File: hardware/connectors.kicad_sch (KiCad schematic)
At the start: 22 parts, among them IC1 API7721FSB-13, J1 FTSH-107-01-L-D-K, J2 USB_C_Receptacle_USB2.0_14P, J25 Conn_01x02, J26 Conn_01x02, J3 SMA, J4 SMA, J5 uFL, J6 uFL, J7 XIAO ESP32S3 Sense, U2 CP2102C-A01-GQFN24R

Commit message: Fixes after review
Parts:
- added C15: 100n, symbol Device:C_Small
- added C16: C_Small, symbol Device:C_Small
- added C17, C26, C27: 10n, symbol Device:C_Small
- added C18, C19: 47p, symbol Device:C_Small
- added D6, D7: LED, symbol Device:LED
- added IC2: FT231XS-U, Package_SO:SSOP-20_3.9x8.7mm_P0.635mm, symbol FT231XS-U:FT231XS-U
- added R13, R14: 220R, symbol Device:R
- R2, R6: value 1k -> 27R
- R3, R4, R5, U2: now not fitted; now left out of the parts list
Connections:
- net +3.3V: now also C27.1
- net 3V3_USB: now also C15.1, C26.1, IC2.13 (3V3OUT), IC2.3 (VCCIO)
- net D+: now also C19.1, IC2.11 (USBDP)
- net D-: now also C18.1, IC2.12 (USBDM)
- net GND: now also C27.2, D6.1 (K), D7.1 (K); no longer J3.2 (Ext), J3.3 (Ext), J3.4 (Ext), J3.5 (Ext), J4.2 (Ext), J4.3 (Ext), J4.4 (Ext), J4.5 (Ext), J5.2 (Ext), J5.3 (Ext), J5.4 (Ext), J5.5 (Ext), J6.2 (Ext), J6.3 (Ext), J6.4 (Ext), J6.5 (Ext)
- net GND_USB: now also C15.2, C16.1, C17.2, C18.2, C19.2, C26.2, IC2.16 (GND_2), IC2.6 (GND_1)
- net ISO_RX: now also IC2.4 (RXD)
- net ISO_TX: now also IC2.20 (TXD)
- net VBUS: now also C17.1, IC2.15 (VCC)
- new net: D7.2 (A), R14.1
- new net: J6.2 (Ext), J6.3 (Ext), J6.4 (Ext), J6.5 (Ext)
- new net: D6.2 (A), R13.1
- new net: J5.2 (Ext), J5.3 (Ext), J5.4 (Ext), J5.5 (Ext)
- new net: J3.2 (Ext), J3.3 (Ext), J3.4 (Ext), J3.5 (Ext)
- new net: J4.2 (Ext), J4.3 (Ext), J4.4 (Ext), J4.5 (Ext)
- new net RXLED: IC2.10 (CBUS2), R13.2
- new net TXLED: IC2.17 (CBUS1), R14.2
- new net USB_RST: IC2.14 (RESET#)
- no-connect marks 27 -> 39
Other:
- note added: "backup if FT231XS will be out of stock"
- note removed: "Question 1 -------> If not these connectors below but Harwin, should I throw away all of these and copy Harwin from ams master? I am unsure about pins assignment, because frontbox has it completely different than ams master."
- moved on the sheet: D13, D14, D15, D2, D3, D4, IC1, J1, J25, J26, J3, J4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

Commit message: Added pi-filter to VANT and added socket for battery
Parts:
- D2: value ~ -> (none)

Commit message: Fixes after review and mouser links for most components added
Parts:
- removed C15: 100n, symbol Device:C_Small
- removed C16: C_Small, symbol Device:C_Small
- removed J2: USB_C_Receptacle_USB2.0_14P, symbol Connector:USB_C_Receptacle_USB2.0_14P
- removed R2, R6: 27R, symbol Device:R
- removed R3: 22.1k, symbol Device:R
- removed R4: 47.5k, symbol Device:R
- removed R5: 1k, symbol Device:R
- removed U2: CP2102C-A01-GQFN24R, QFN50P400X400X80-25N-D, symbol CP2102C-A01-GQFN24R:CP2102C-A01-GQFN24R
- added C13: 100nF, Capacitor_SMD:C_0603_1608Metric_Pad1.08x0.95mm_HandSolder, symbol Device:C_Small
- added D2, D8: SMF5.0A, 5Vtvs:SODFL3618X110N, symbol Diode:SMF5V0A
- added FB1: 40R@100MHz, FerriteUSB:BEADC2012X110N, symbol Device:FerriteBead_Small
- added J7: USB_A, USBAconnector:UE27AC5410H, symbol Connector:USB_A
- added R10, R11: 27R, Resistor_SMD:R_0603_1608Metric_Pad0.98x0.95mm_HandSolder, symbol Device:R
- added R12: 10k, Resistor_SMD:R_0603_1608Metric_Pad0.98x0.95mm_HandSolder, symbol Device:R
- C12: renamed from C17; value 10n -> 10nF; footprint (none) -> Capacitor_SMD:C_0603_1608Metric_Pad1.08x0.95mm_HandSolder; Mouser (none) -> https://www.mouser.pl/ProductDetail/Murata-Electronics/GCM1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
- C14: renamed from C26; value 10n -> 10nF; footprint (none) -> Capacitor_SMD:C_0603_1608Metric_Pad1.08x0.95mm_HandSolder; Mouser (none) -> https://www.mouser.pl/ProductDetail/Murata-Electronics/GCM1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
- C16: renamed from C27; value 10n -> 10nF; footprint (none) -> Capacitor_SMD:C_0603_1608Metric_Pad1.08x0.95mm_HandSolder; Mouser (none) -> https://www.mouser.pl/ProductDetail/Murata-Electronics/GCM1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
- C24: renamed from C18; value 47p -> 47pF; now not fitted
- C25: renamed from C19; value 47p -> 47pF; now not fitted
- D10: renamed from D14; value STS232050B751 -> 5V/360W
- D11: renamed from D15; value 3.6V/400W -> 3.6V/85W
- D6: renamed from D13; value STS232050B751 -> (none); footprint Package_TO_SOT_SMD:SOT-23_Handsoldering -> (none); Manufacturer_Part_Number STS232050B751 -> (none); Mouser https://www.mouser.pl/ProductDetail/Eaton-Electronics/STS23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 -> (none); Mouser No 504-STS232050B751 -> (none)
- D9: renamed from D4; value STS232050B751 -> 5V/360W
- J2: renamed from J5; value uFL -> uFL ant
- J3: value SMA -> SMA ant
- J4: renamed from J6; value uFL -> uFL ant
- J5: renamed from J4; value SMA -> SMA ant
- J9: renamed from J7; Mouser (none) -> ---
- R13, R14: value 220R -> 330R; footprint (none) -> Resistor_SMD:R_0603_1608Metric_Pad0.98x0.95mm_HandSolder; Mouser (none) -> https://www.mouser.pl/ProductDetail/Vishay-Draloric/RCS0603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
- U4: renamed from IC2; Mouser (none) -> https://www.mouser.pl/ProductDetail/FTDI/FT231XS-R?qs=Gp1Yz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
- U5: renamed from IC1; Mouser (none) -> https://www.mouser.pl/ProductDetail/Diodes-Incorporated/API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
- renumbered D2 to D3, D6 to D4, D7 to D5, D3 to D7, J25 to J1, J26 to J6, J1 to J8
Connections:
- net +5V: now also D8.1 (A1)
- net 3V3_USB: now also R13.2, R14.2, C13.1, R12.1
- net D+: now also J7.3 (D+), R11.2; no longer U4.11 (USBDP)
- net D-: now also J7.2 (D-), R10.2; no longer U4.12 (USBDM)
- net GND: now also D8.2 (A2); no longer D4.1 (K), D5.1 (K)
- net GND_USB: now also C13.2, D2.2 (A2), J7.4 (GND), J7.SH (Shield)
- net RXLED: now also D4.1 (K); no longer R13.2
- net TXLED: now also D5.1 (K); no longer R14.2
- net USB_RST: now also R12.2
- net VBUS: now also FB1.2; no longer C12.1
- net at J4.2 (Ext), J4.3 (Ext), J4.4 (Ext)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: now also J5.2 (Ext), J5.3 (Ext), J5.4 (Ext), J5.5 (Ext)
- net at J2.2 (Ext), J2.3 (Ext), J2.4 (Ext)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: now also J3.2 (Ext), J3.3 (Ext), J3.4 (Ext), J3.5 (Ext)
- new net: R10.1, U4.12 (USBDM)
- new net: C12.1, D2.1 (A1), FB1.1, J7.1 (VBUS)
- new net: R11.1, U4.11 (USBDP)
- no-connect marks 39 -> 21
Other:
- moved on the sheet: C12, D3, D4, D5, D7, J2, J3, J5, J9, R13, U4

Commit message: changed some elements on shematic
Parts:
- added D15, D16: SMF5.0A, 5Vtvs:SODFL3618X110N, symbol Diode:SMF5V0A
- C24, C25: footprint (none) -> DoNotPopulate; Mouser (none) -> --
- D3: value (none) -> 5V/140W; footprint (none) -> Package_TO_SOT_SMD:SOT-23-3; Mouser (none) -> https://www.mouser.pl/ProductDetail/STMicroelectronics/ESDA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
- D4, D5: footprint (none) -> Diode_SMD:D_0603_1608Metric_Pad1.05x0.95mm_HandSolder; Mouser (none) -> https://www.mouser.pl/ProductDetail/Wurth-Elektronik/150060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
- D6: value (none) -> 27V/420W; footprint (none) -> Package_TO_SOT_SMD:SOT-23-3; Mouser (none) -> https://www.mouser.pl/ProductDetail/Micro-Commercial-Compon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
- D7: Mouser (none) -> https://www.mouser.pl/ProductDetail/onsemi/NSVRB751V40T1G?q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; Mouser Part Number 863-NSVRB751V40T1G -> (none); Mouser Price/Stock https://www.mouser.pl/ProductDetail/onsemi/NSVRB751V40T1G?q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 -> (none)
- D8: value SMF5.0A -> 5V/200W
- J7: footprint USBAconnector:UE27AC5410H -> USBAconnector:UJ2AV4TH; Mouser https://www.mouser.pl/ProductDetail/Amphenol-Commercial-Pro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 -> https://www.mouser.pl/ProductDetail/Same-Sky/UJ2-AV-4-TH?qs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
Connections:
- net D+: no longer D3.2 (A2)
- net D-: no longer D3.1 (A1)
- net d-: now reaches R10.1, U4.12 (USBDM)
- net d-: now also D3.1 (A1)
- net d+: now reaches R11.1, U4.11 (USBDP)
- net d+: now also D3.2 (A2)
- net at J4.1 (In), J5.1 (In): now also D15.1 (A1)
- net at J4.2 (Ext), J4.3 (Ext), J4.4 (Ext)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: now also D15.2 (A2)
- net at J2.1 (In), J3.1 (In): now also D16.1 (A1)
- net at J2.2 (Ext), J2.3 (Ext), J2.4 (Ext)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: now also D16.2 (A2)
- net +24V renamed +24V_EXT
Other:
- note removed: "backup if FT231XS will be out of stock"
- moved on the sheet: C14, C16, J2, J3, J4, J5, U5

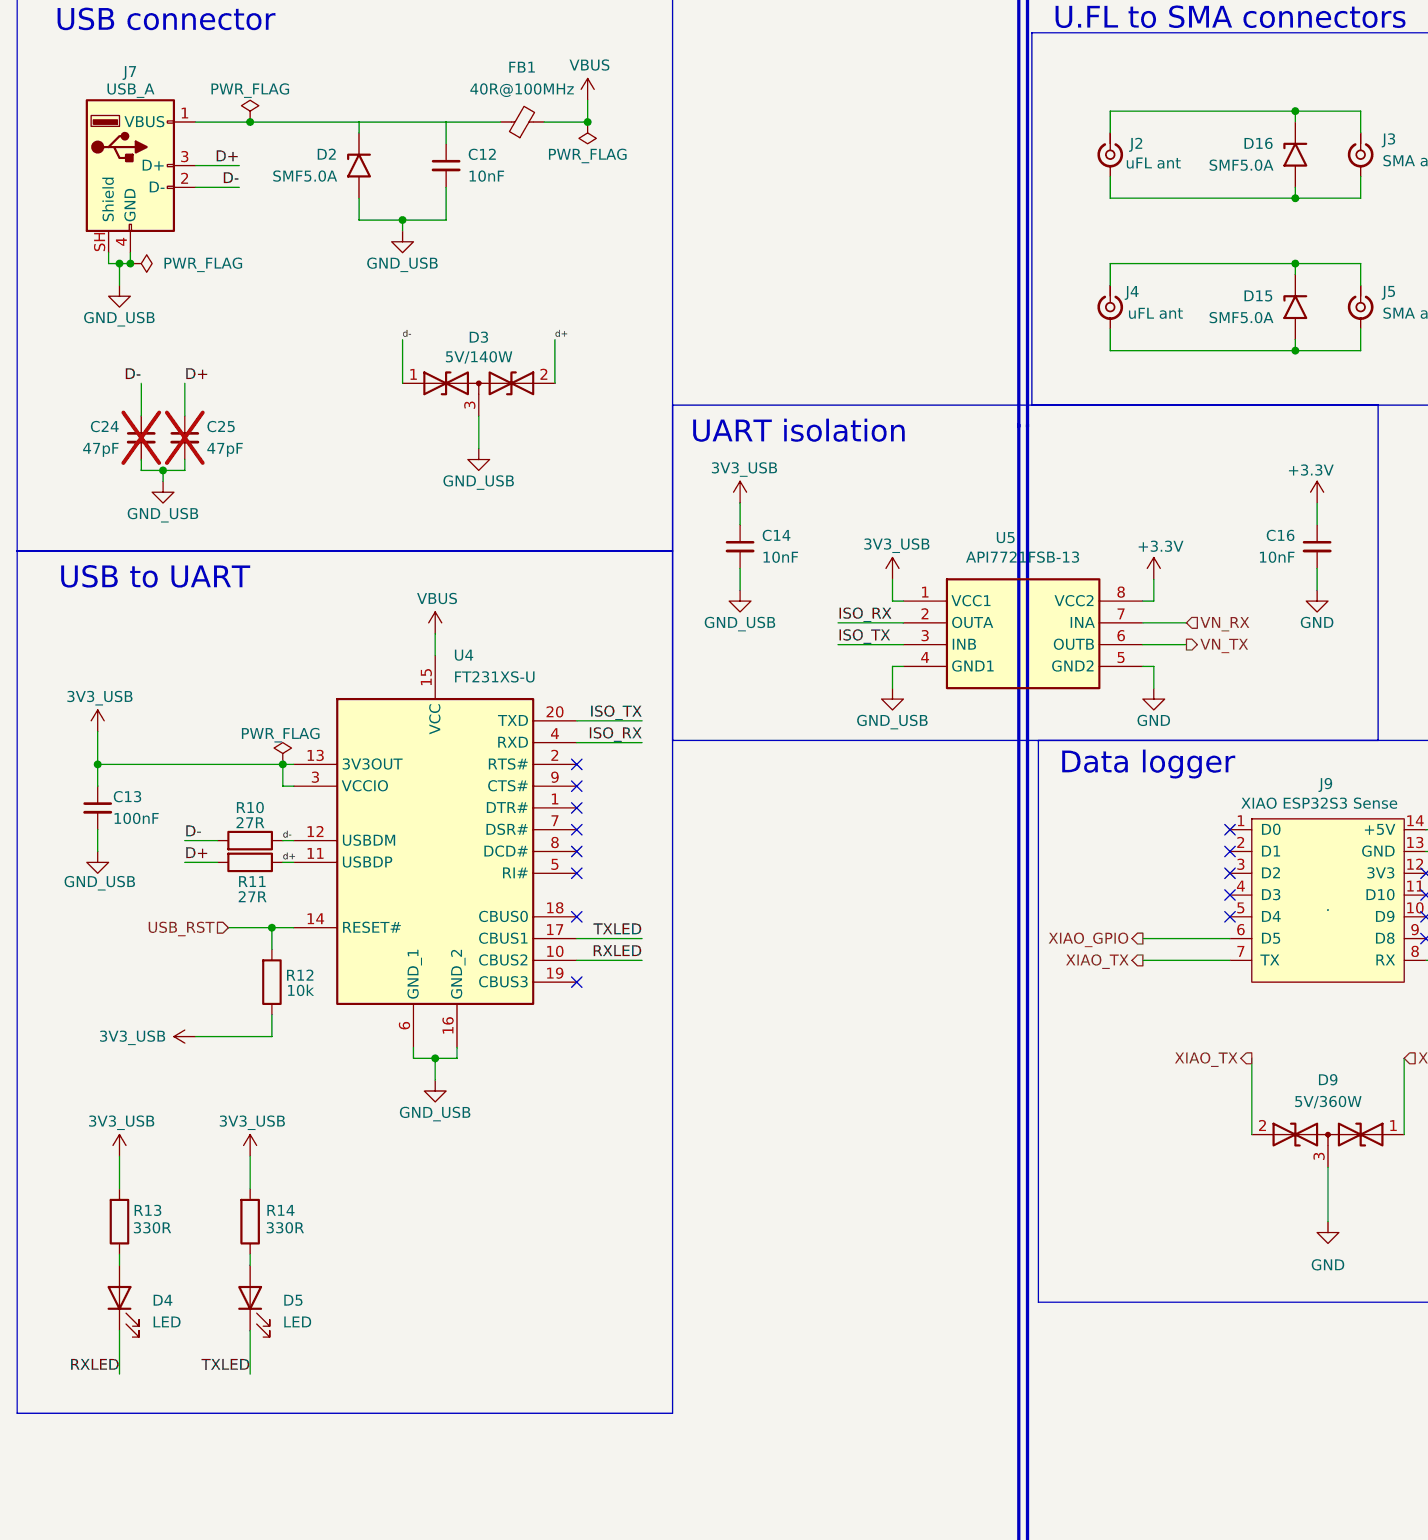
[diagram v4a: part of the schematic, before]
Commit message: 3D models, optocoupler added, pcb settings and components placing
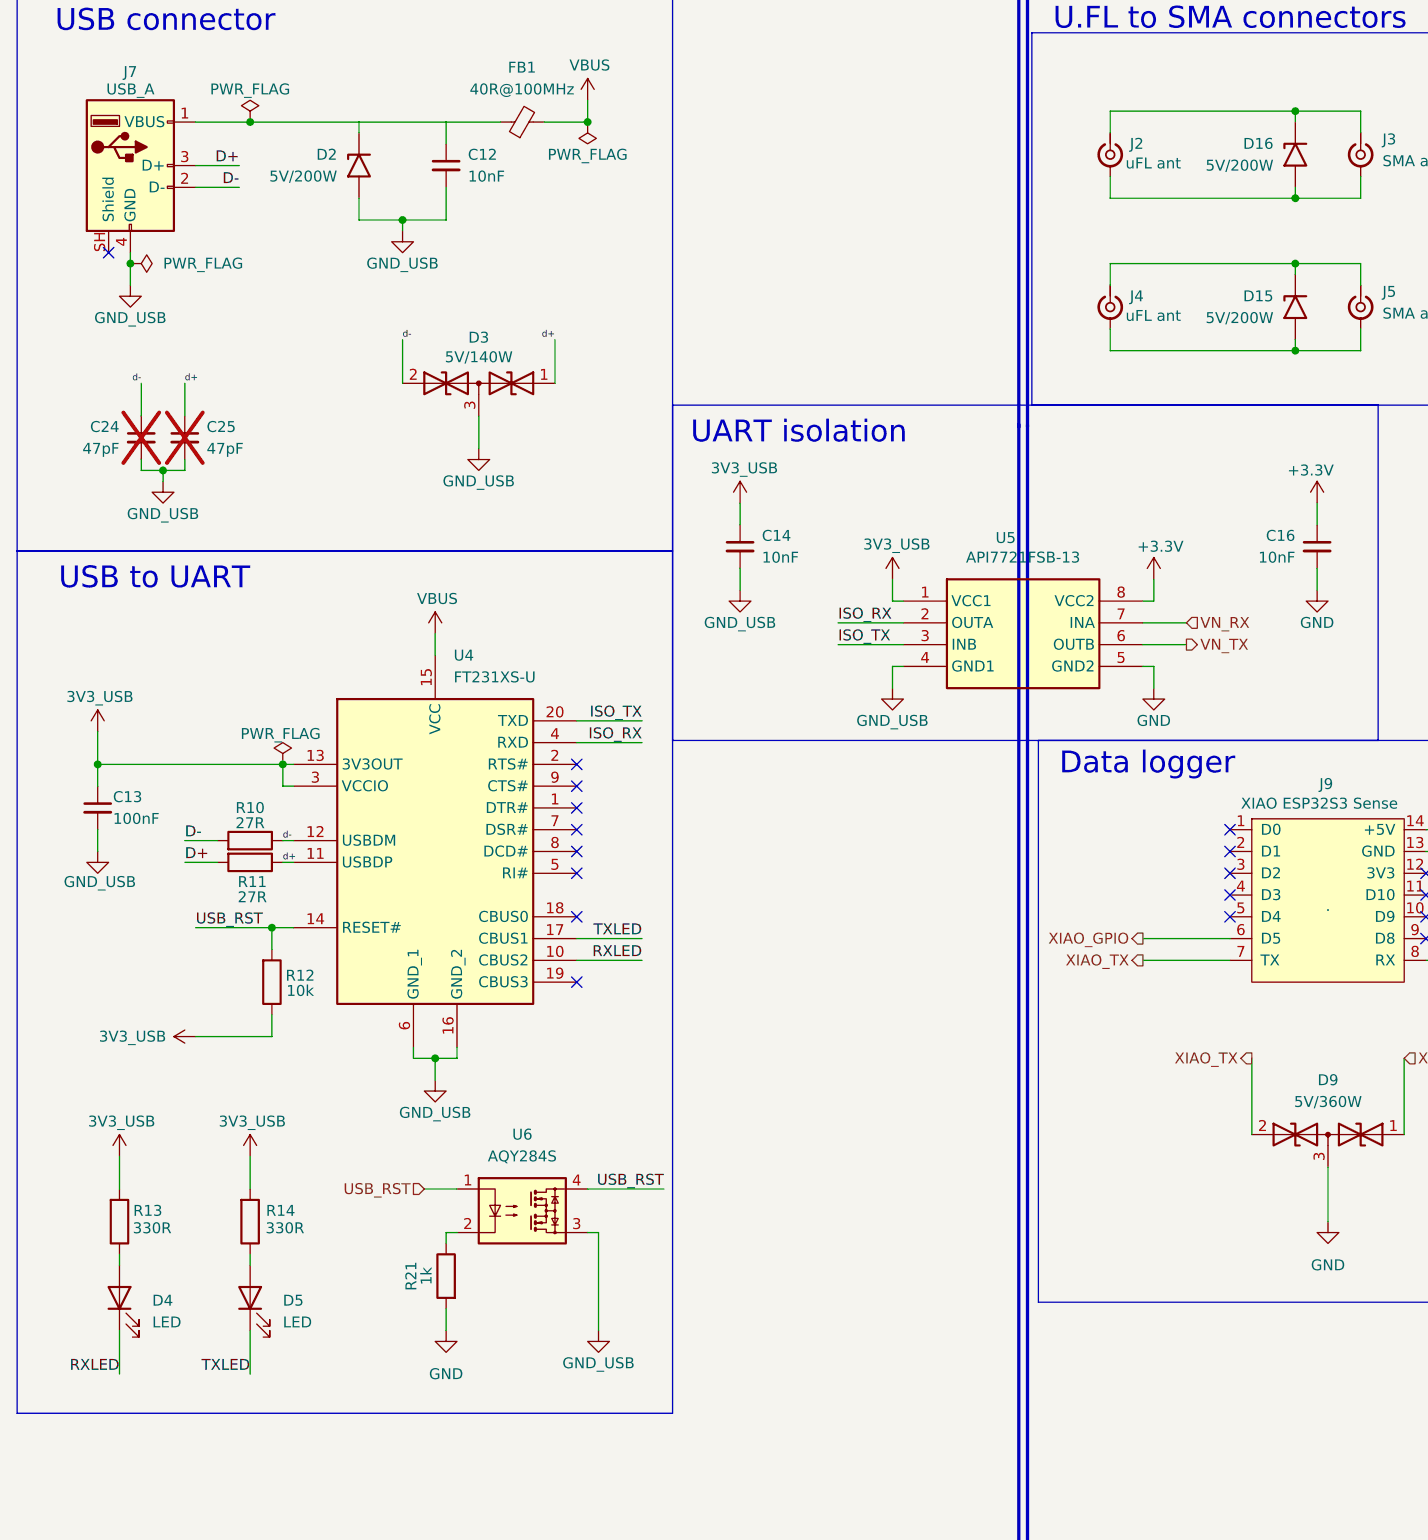
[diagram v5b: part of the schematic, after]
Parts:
- added R21: 1k, Resistor_SMD:R_0603_1608Metric_Pad0.98x0.95mm_HandSolder, symbol Device:R
- added U6: AQY284S, OptoCoupler:SOP254P680X230-4N, symbol Relay_SolidState:AQY284S
- C24, C25: footprint DoNotPopulate -> Capacitor_SMD:C_0603_1608Metric_Pad1.08x0.95mm_HandSolder
- D15, D16, D2: value SMF5.0A -> 5V/200W
- J1, J6: footprint StrainRelief:Wire_StrainRelief -> StrainRelief:StrainRelief
- J8: footprint Samacsys:FTSH-107-XX-YYY-D-K -> samacsys:FTSH-107-XX-YYY-D-K
- J9: footprint Samacsys:XIAO-ESP32S3-DIP -> samacsys:XIAO-ESP32S3-DIP
- U5: footprint SOIC127P1150X280-8N -> iso_conv:SOIC127P1150X280-8N; Height 2.8 -> (none); Manufacturer_Name Diodes Incorporated -> (none); Manufacturer_Part_Number API7721FSB-13 -> (none)
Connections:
- net D+: no longer C25.1
- net D-: no longer C24.1
- net GND: now also R21.2
- net GND_USB: now also U6.3; no longer J7.SH (Shield)
- net USB_RST: now also U6.1, U6.4
- net d+: now also C25.1, D3.1 (A1); no longer D3.2 (A2)
- net d-: now also C24.1, D3.2 (A2); no longer D3.1 (A1)
- net at D15.2 (A2), J4.2 (Ext), J4.3 (Ext)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: no longer J4.4 (Ext), J4.5 (Ext)
- net at D16.2 (A2), J2.2 (Ext), J2.3 (Ext)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: no longer J2.4 (Ext), J2.5 (Ext)
- new net: R21.1, U6.2
- no-connect marks 21 -> 22

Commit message: All components placed on pcb
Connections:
- net PROG_SWCLK: now also D11.3 (K); no longer D11.4 (K)
- net PROG_SWDIO: now also D11.4 (K); no longer D11.3 (K)
- net USB_RST: no longer R12.2, U4.14 (RESET#), U6.4
- net XIAO_RX: now also D9.2 (A2); no longer D9.1 (A1)
- net XIAO_TX: now also D9.1 (A1); no longer D9.2 (A2)
- new net usbRST: R12.2, U4.14 (RESET#), U6.4
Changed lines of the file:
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@@
 		)
 	)
+	(label "PROG_SWCLK"
+		(at 261.62 135.89 90)
+		(effects
+			(font
+				(size 1.27 1.27)
+			)
+			(justify left bottom)
+		)
+	)
 	(label "ISO_RX"
 		(at 107.95 86.36 0)
@@
 		)
 	)
-	(label "USB_RST"
+	(label "usbRST"
 		(at 87.63 152.4 180)
 		(effects
@@
 		)
 	)
-	(label "PROG_SWCLK"
-		(at 264.16 135.89 90)
-		(effects
-			(font
-				(size 1.27 1.27)
-			)
-			(justify left bottom)
-		)
-	)
 	(label "PROG_RX"
 		(at 220.98 110.49 0)
@@
 		)
 	)
-	(label "USB_RST"
+	(label "usbRST"
 		(at 33.02 121.92 0)
 		(effects
@@
 		)
 	)
-	(label "PROG_SWDIO"
-		(at 261.62 135.89 90)
-		(effects
-			(font
-				(size 1.27 1.27)
-			)
-			(justify left bottom)
-		)
-	)
 	(label "d-"
 		(at 43.18 111.76 0)
@@
 		)
 	)
+	(label "PROG_SWDIO"
+		(at 264.16 135.89 90)
+		(effects
+			(font
+				(size 1.27 1.27)
+			)
+			(justify left bottom)
+		)
+	)
 	(label "CAN-"
 		(at 274.32 22.86 0)
@@
 		(lib_id "Device:D_TVS_Dual_AAC")
 		(at 165.1 146.05 0)
-		(mirror y)
 		(unit 1)
 		(body_style 1)
@@
 		)
 		(property "Footprint" "Package_TO_SOT_SMD:SOT-23_Handsoldering"
-			(at 168.91 146.05 0)
+			(at 161.29 146.05 0)
 			(hide yes)
 			(show_name no)
@@
 		)
 		(property "Datasheet" "https://www.eaton.com/content/dam/eaton/products/electronic-components/resources/data-sheet/eaton-sts232xxxbxxx-tvs-diode-array-esd-suppressor-data-sheet.pdf"
-			(at 168.91 146.05 0)
+			(at 161.29 146.05 0)
 			(hide yes)
 			(show_name no)

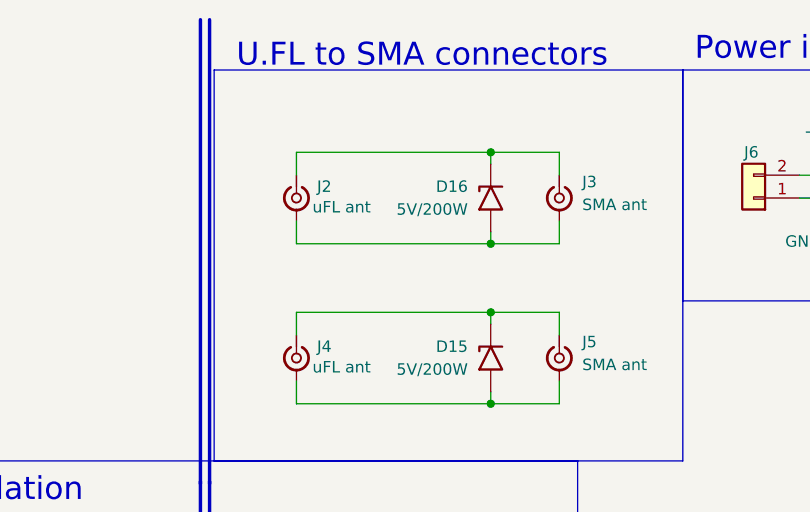
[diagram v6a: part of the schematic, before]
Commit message: MCU and VN-300 routed
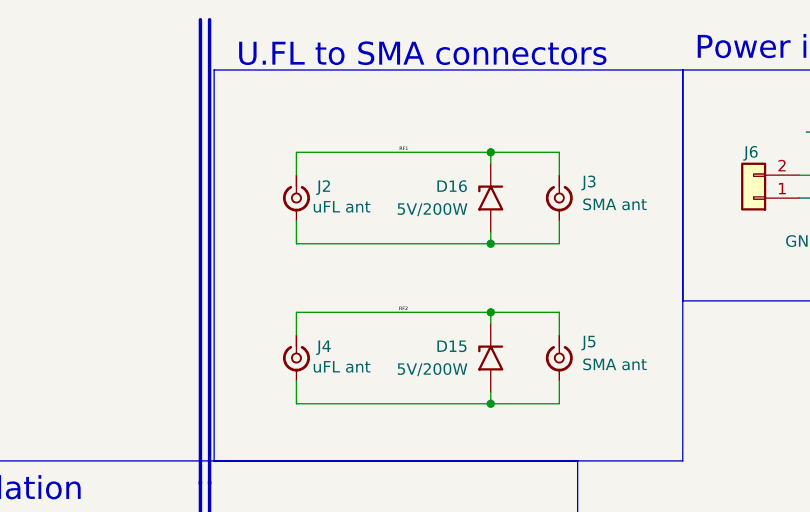
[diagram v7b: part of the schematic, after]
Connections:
- net RF2: now reaches D15.1 (A1), J4.1 (In), J5.1 (In)
- net RF1: now reaches D16.1 (A1), J2.1 (In), J3.1 (In)
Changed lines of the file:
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@@
+		)
+	)
+	(label "RF2"
+		(at 151.0981 44.45 0)
+		(effects
+			(font
+				(size 0.381 0.381)
+			)
+			(justify left bottom)
 		)
 	)
@@
 			)
 			(justify left bottom)
+		)
+	)
+	(label "RF1"
+		(at 151.13 26.67 0)
+		(effects
+			(font
+				(size 0.381 0.381)
+			)
+			(justify left bottom)

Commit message: Finished pcb routing
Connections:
- net CAN+: now also D6.2 (A2); no longer D6.1 (A1)
- net CAN-: now also D6.1 (A1); no longer D6.2 (A2)
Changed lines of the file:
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@@
 		(lib_id "Device:D_TVS_Dual_AAC")
 		(at 265.43 27.94 0)
+		(mirror y)
 		(unit 1)
 		(body_style 1)
@@
 		)
 		(property "Footprint" "Package_TO_SOT_SMD:SOT-23-3"
-			(at 261.62 27.94 0)
+			(at 269.24 27.94 0)
 			(hide yes)
 			(show_name no)
@@
 		)
 		(property "Datasheet" "https://www.mouser.pl/datasheet/3/225/1/ESD27VT2BHE3_SOT_23.pdf"
-			(at 261.62 27.94 0)
+			(at 269.24 27.94 0)
 			(hide yes)
 			(show_name no)
